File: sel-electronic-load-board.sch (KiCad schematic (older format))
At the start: 55 parts

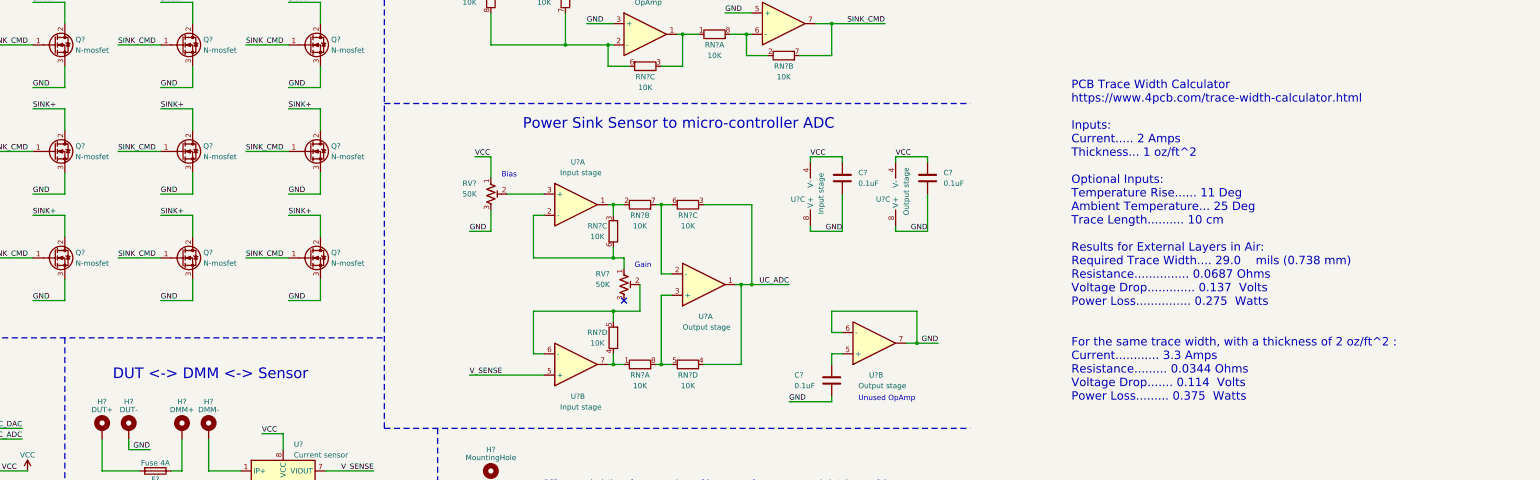
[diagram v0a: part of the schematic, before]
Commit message: Schematic almost done, need to provision pin6 of current sensor to GND
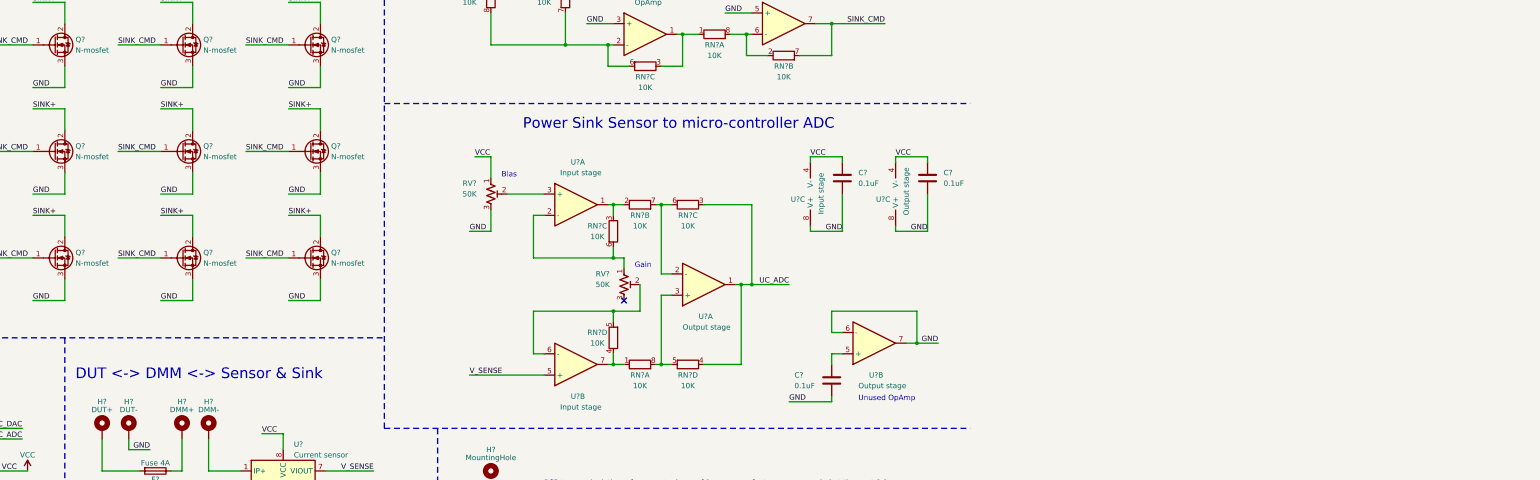
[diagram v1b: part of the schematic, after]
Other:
- note added: "DUT <-> DMM <-> Sensor & Sink"
- note removed: "DUT <-> DMM <-> Sensor"
- note removed: "PCB Trace Width Calculator\nhttps://www.4pcb.com/trace-width-calculator.html\n\nInputs:\nCurrent..... 2 Amps\nThickness... 1 oz/ft^2\n\nOptional Inputs:\nTemperature Rise...... 11 Deg\nAmbient Temperature... 25 Deg\nTrace Length.......... 10 cm\n\nResults for External Layers in Air:\nRequired Trace Width.... 29.0 mils (0.738 mm)\nResistance............... 0.0687 Ohms\nVoltage Drop............. 0.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"
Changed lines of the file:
@@
 Wire Notes Line
 	5500 3050 11000 3050
-Text Notes 11950 5850 0    79   ~ 0
-PCB Trace Width Calculator\nhttps://www.4pcb.com/trace-width-calculator.html\n\nInputs:\nCurrent..... 2 Amps\nThickness... 1 oz/ft^2\n\nOptional Inputs:\nTemperature Rise...... 11 Deg\nAmbient Temperature... 25 Deg\nTrace Length.......... 10 cm\n\nResults for External Layers in Air:\nRequired Trace Width.... 29.0    mils (0.738 mm)\nResistance............... 0.0687 Ohms\nVoltage Drop............. 0.137  Volts\nPower Loss............... 0.275  Watts\n\n\nFor the same trace width, with a thickness of 2 oz/ft^2 :\nCurrent............ 3.3 Amps\nResistance......... 0.0344 Ohms\nVoltage Drop....... 0.114  Volts\nPower Loss......... 0.375  Watts\n
 Wire Notes Line
 	5500 6100 11000 6100
@@
 Wire Wire Line
 	3850 6800 4150 6800
-Text Notes 2950 5650 0    100  ~ 0
-DUT <-> DMM <-> Sensor
+Text Notes 2600 5650 0    100  ~ 0
+DUT <-> DMM <-> Sensor & Sink
 $Comp
 L Connector_Generic:Conn_02x05_Odd_Even J?

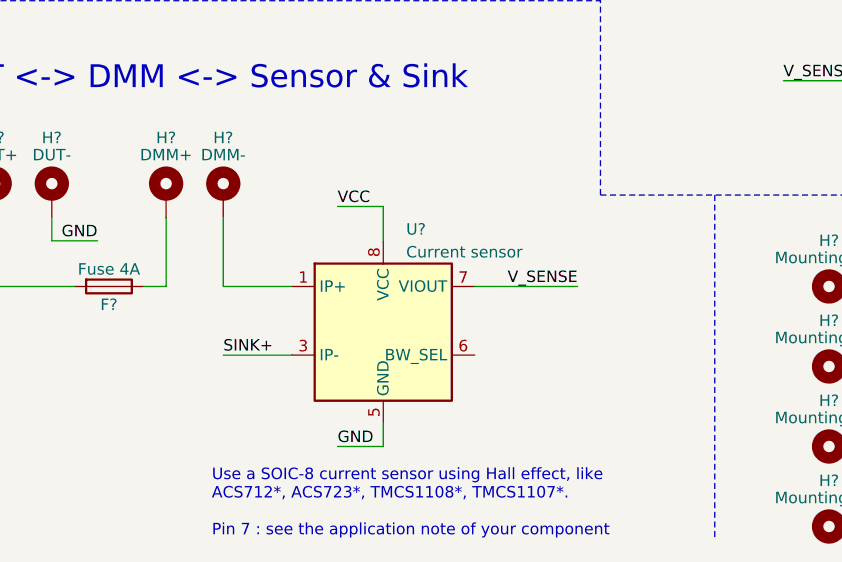
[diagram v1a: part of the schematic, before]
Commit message: implement a bypass of the external DMM
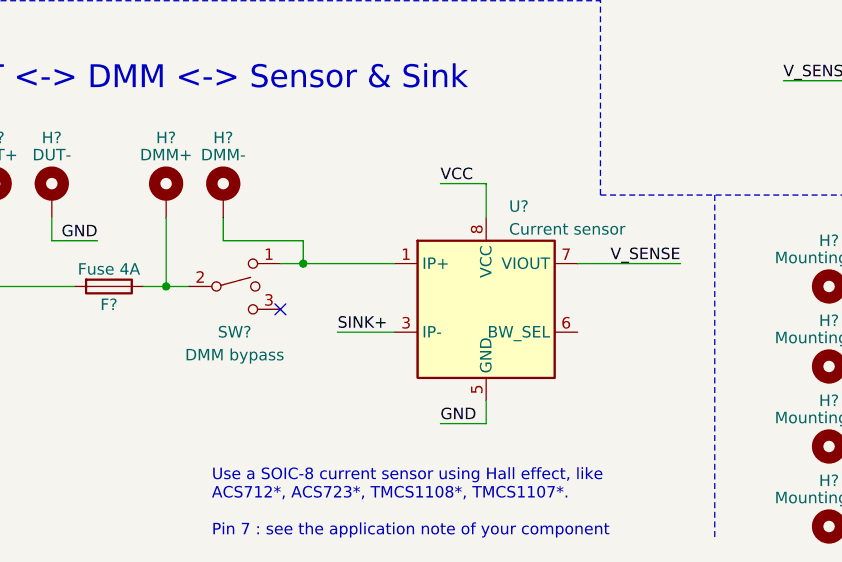
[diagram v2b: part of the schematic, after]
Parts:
- added SW?: DMM bypass, symbol Switch:SW_SPDT_MSM
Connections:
- net at F?.1, H?.1: now also SW?.2
- net at H?.1, U?.1 (IP+), U?.2 (IP+): now also SW?.1
- no-connect marks 1 -> 2
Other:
- moved on the sheet: U?
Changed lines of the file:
@@
 L Sensor_Current:ACS723xLCTR-10AB U?
 U 1 1 62897256
-P 4550 6700
-F 0 "U?" H 4650 7150 50  0000 L CNN
-F 1 "Current sensor" H 4650 7050 50  0000 L CNN
-F 2 "Package_SO:SOIC-8_3.9x4.9mm_P1.27mm" H 4650 6350 50  0001 L CIN
-F 3 "http://www.allegromicro.com/~/media/Files/Datasheets/ACS723-Datasheet.ashx?la=en" H 4550 6700 50  0001 C CNN
-	1    4550 6700
-	1    0    0    -1
-$EndComp
-Text Label 3850 6800 0    50   ~ 0
+P 5000 6600
+F 0 "U?" H 5100 7050 50  0000 L CNN
+F 1 "Current sensor" H 5100 6950 50  0000 L CNN
+F 2 "Package_SO:SOIC-8_3.9x4.9mm_P1.27mm" H 5100 6250 50  0001 L CIN
+F 3 "http://www.allegromicro.com/~/media/Files/Datasheets/ACS723-Datasheet.ashx?la=en" H 5000 6600 50  0001 C CNN
+	1    5000 6600
+	1    0    0    -1
+$EndComp
+Text Label 4350 6700 0    50   ~ 0
 SINK+
-Text Label 5400 6500 2    50   ~ 0
+Text Label 5850 6400 2    50   ~ 0
 V_SENSE
 Wire Wire Line
-	4950 6500 5400 6500
-Text Label 4350 6150 0    50   ~ 0
+	5400 6400 5850 6400
+Text Label 4800 6050 0    50   ~ 0
 VCC
 Text Label 3300 6300 2    50   ~ 0
 GND
 Wire Wire Line
-	4350 6150 4550 6150
-Wire Wire Line
-	4550 6150 4550 6300
-Wire Wire Line
-	4350 7200 4550 7200
-Wire Wire Line
-	4550 7200 4550 7100
+	4800 6050 5000 6050
+Wire Wire Line
+	5000 6050 5000 6200
+Wire Wire Line
+	4800 7100 5000 7100
+Wire Wire Line
+	5000 7100 5000 7000
 Text Notes 3800 7600 0    50   ~ 0
 Use a SOIC-8 current sensor using Hall effect, like \nACS712*, ACS723*, TMCS1108*, TMCS1107*.\n\nPin 7 : see the application note of your component
@@
 	3500 6500 3600 6500
 Wire Wire Line
-	4150 6500 3850 6500
-Wire Wire Line
 	2850 6200 2850 6500
 Wire Wire Line
@@
 Wire Wire Line
 	3600 6200 3600 6500
-Wire Wire Line
-	3850 6200 3850 6500
-Text Label 4350 7200 0    50   ~ 0
+Text Label 4800 7100 0    50   ~ 0
 GND
-Wire Wire Line
-	3850 6800 4150 6800
 Text Notes 2600 5650 0    100  ~ 0
 DUT <-> DMM <-> Sensor & Sink
@@
 Text Notes 7000 7050 0    50   ~ 0
 PCB trace calculations, for an outer layer of 1 ounce per foot square ; rounded at the next 0.1mm.\n\n1A --> 0.3mm\n2A --> 0.8mm\n3A --> 1.4mm\n4A --> 2.1mm\n
+$Comp
+L Switch:SW_SPDT_MSM SW?
+U 1 1 62A98008
+P 3900 6500
+F 0 "SW?" H 3900 6300 50  0000 C CNN
+F 1 "DMM bypass" H 3900 6200 50  0000 C CNN
+F 2 "" H 3900 6500 50  0001 C CNN
+F 3 "~" H 3900 6500 50  0001 C CNN
+	1    3900 6500
+	1    0    0    -1
+$EndComp
+Wire Wire Line
+	3600 6500 3700 6500
+Connection ~ 3600 6500
+Wire Wire Line
+	4200 6400 4600 6400
+Wire Wire Line
+	4200 6400 4100 6400
+Connection ~ 4200 6400
+NoConn ~ 4100 6600
+Wire Wire Line
+	4350 6700 4600 6700
+Wire Wire Line
+	3850 6200 3850 6300
+Wire Wire Line
+	3850 6300 4200 6300
+Wire Wire Line
+	4200 6300 4200 6400
 $EndSCHEMATC

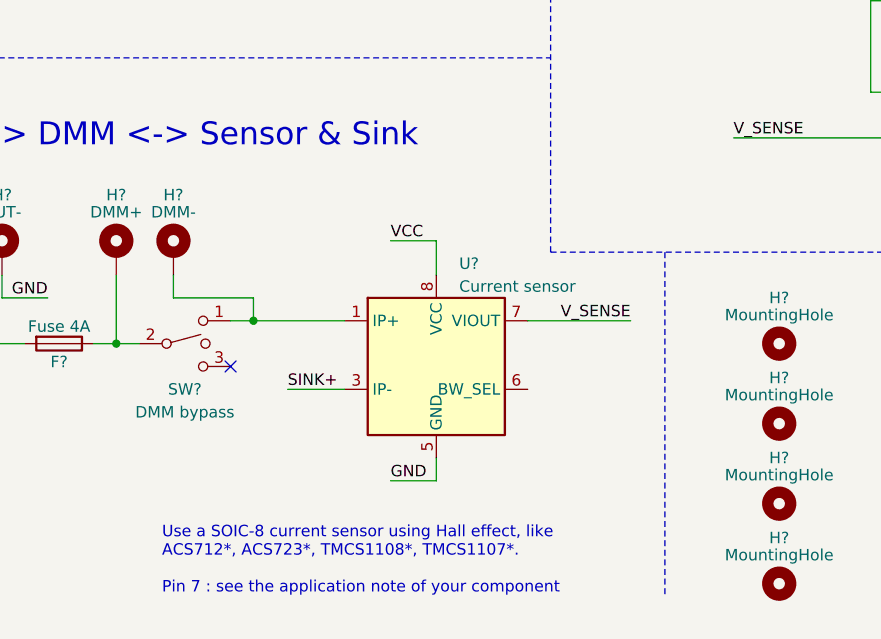
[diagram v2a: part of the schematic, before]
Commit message: Finished the current sensor IC
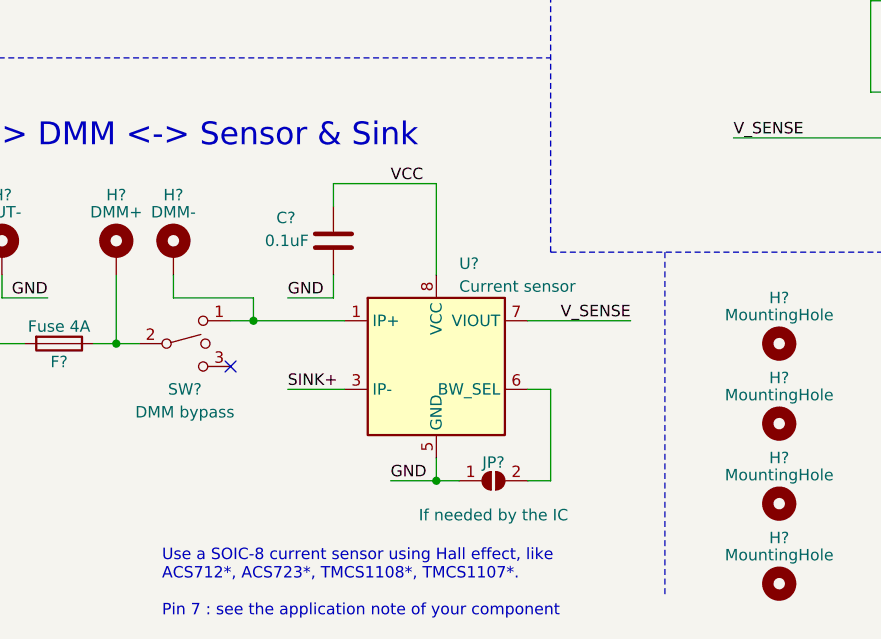
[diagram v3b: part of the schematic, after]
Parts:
- added C?: 0.1uF, Capacitor_SMD:C_1206_3216Metric_Pad1.33x1.80mm_HandSolder, symbol Device:C
- added JP?: If needed by the IC, symbol Jumper:SolderJumper_2_Open
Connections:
- net GND: now also C?.2, JP?.1 (A)
- net VCC: now also C?.1
- net at U?.6 (BW_SEL): now also JP?.2 (B)
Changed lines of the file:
@@
 Wire Wire Line
 	5400 6400 5850 6400
-Text Label 4800 6050 0    50   ~ 0
+Text Label 4800 5800 0    50   ~ 0
 VCC
 Text Label 3300 6300 2    50   ~ 0
 GND
 Wire Wire Line
-	4800 6050 5000 6050
-Wire Wire Line
-	5000 6050 5000 6200
-Wire Wire Line
 	4800 7100 5000 7100
 Wire Wire Line
 	5000 7100 5000 7000
-Text Notes 3800 7600 0    50   ~ 0
+Text Notes 3800 7700 0    50   ~ 0
 Use a SOIC-8 current sensor using Hall effect, like \nACS712*, ACS723*, TMCS1108*, TMCS1107*.\n\nPin 7 : see the application note of your component
 $Comp
@@
 Wire Wire Line
 	4200 6300 4200 6400
+$Comp
+L Device:C C?
+U 1 1 62B12721
+P 4550 6050
+AR Path="/627E1114/617D5FF5/62B12721" Ref="C?"  Part="1"
+AR Path="/62B12721" Ref="C?"  Part="1"
+F 0 "C?" H 4300 6150 50  0000 L CNN
+F 1 "0.1uF" H 4250 6050 50  0000 L CNN
+F 2 "Capacitor_SMD:C_1206_3216Metric_Pad1.33x1.80mm_HandSolder" H 4588 5900 50  0001 C CNN
+F 3 "~" H 4550 6050 50  0001 C CNN
+	1    4550 6050
+	1    0    0    -1
+$EndComp
+Wire Wire Line
+	4350 6300 4550 6300
+Text Label 4350 6300 0    50   ~ 0
+GND
+Wire Wire Line
+	5000 5800 5000 6200
+$Comp
+L Jumper:SolderJumper_2_Open JP?
+U 1 1 62B47189
+P 5250 7100
+F 0 "JP?" H 5250 7180 50  0000 C CNN
+F 1 "If needed by the IC" H 5250 6950 50  0000 C CNN
+F 2 "" H 5250 7100 50  0001 C CNN
+F 3 "~" H 5250 7100 50  0001 C CNN
+	1    5250 7100
+	1    0    0    -1
+$EndComp
+Wire Wire Line
+	5000 7100 5100 7100
+Connection ~ 5000 7100
+Wire Wire Line
+	5400 7100 5500 7100
+Wire Wire Line
+	5500 7100 5500 6700
+Wire Wire Line
+	5500 6700 5400 6700
+Wire Wire Line
+	4550 6200 4550 6300
+Wire Wire Line
+	4550 5800 4550 5900
+Wire Wire Line
+	4550 5800 5000 5800
 $EndSCHEMATC

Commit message: annotations
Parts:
- gave numbers to parts that had none: 44
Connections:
- net SINK_CMD: now also RN1.5 (R4.2); no longer RN1.7 (R2.2)
- net UC_ADC: now also RN3.3 (R3.1); no longer RN3.4 (R4.1)
- net at RN1.7 (R2.2), RN1.8 (R1.2), U1.2 (-): now also RN2.8 (R1.2); no longer RN2.6 (R3.2)
- net at RN2.2 (R2.1), U2.1: now also RN2.4 (R4.1); no longer RN2.3 (R3.1)
- net at RV4.1, U2.2 (-): now also RN2.5 (R4.2); no longer RN2.6 (R3.2)
- net at RV4.2, U2.6 (-): now also RN3.8 (R1.2); no longer RN3.5 (R4.2)
- new net: RN1.3 (R3.1), RN2.1 (R1.1), U1.1
- new net: RN1.4 (R4.1), RN1.6 (R3.2), U1.6 (-)
- new net: RN3.1 (R1.1), RN3.2 (R2.1), U2.7
- new net: RN3.6 (R3.2), RN3.7 (R2.2), U3.3 (+)
